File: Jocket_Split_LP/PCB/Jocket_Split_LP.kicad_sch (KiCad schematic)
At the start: 79 parts, among them J2 4PIN, J3 OLED, J4 53780-0270, P1 i2c_pin, P2 i2c_pin, SW1 SW_PUSH_LED, SW10 SW_PUSH_LED, SW11 SW_PUSH_LED, SW12 SW_PUSH_LED, SW13 SW_PUSH_LED, SW14 SW_PUSH_LED, SW15 SW_PUSH_LED, SW16 SW_PUSH_LED, SW17 SW_PUSH_LED, SW18 SW_PUSH_LED, SW19 SW_PUSH_LED, SW2 SW_PUSH_LED, SW20 SW_PUSH_LED, SW21 SW_PUSH_LED, SW22 SW_PUSH_LED, SW23 SW_PUSH_LED, SW24 SW_PUSH_LED, SW25 Rotary_Encoder_Switch, SW26 SW_PUSH_LED, SW27 SW_PUSH_LED, SW28 SW_PUSH_LED, SW29 SW_PUSH_LED, SW3 SW_PUSH_LED, SW30 SW_PUSH_LED, SW4 SW_PUSH_LED, SW5 SW_PUSH_LED, SW6 SW_PUSH_LED, SW7 SW_PUSH_LED, SW8 SW_PUSH_LED, SW9 SW_PUSH_LED, U1 ProMicro

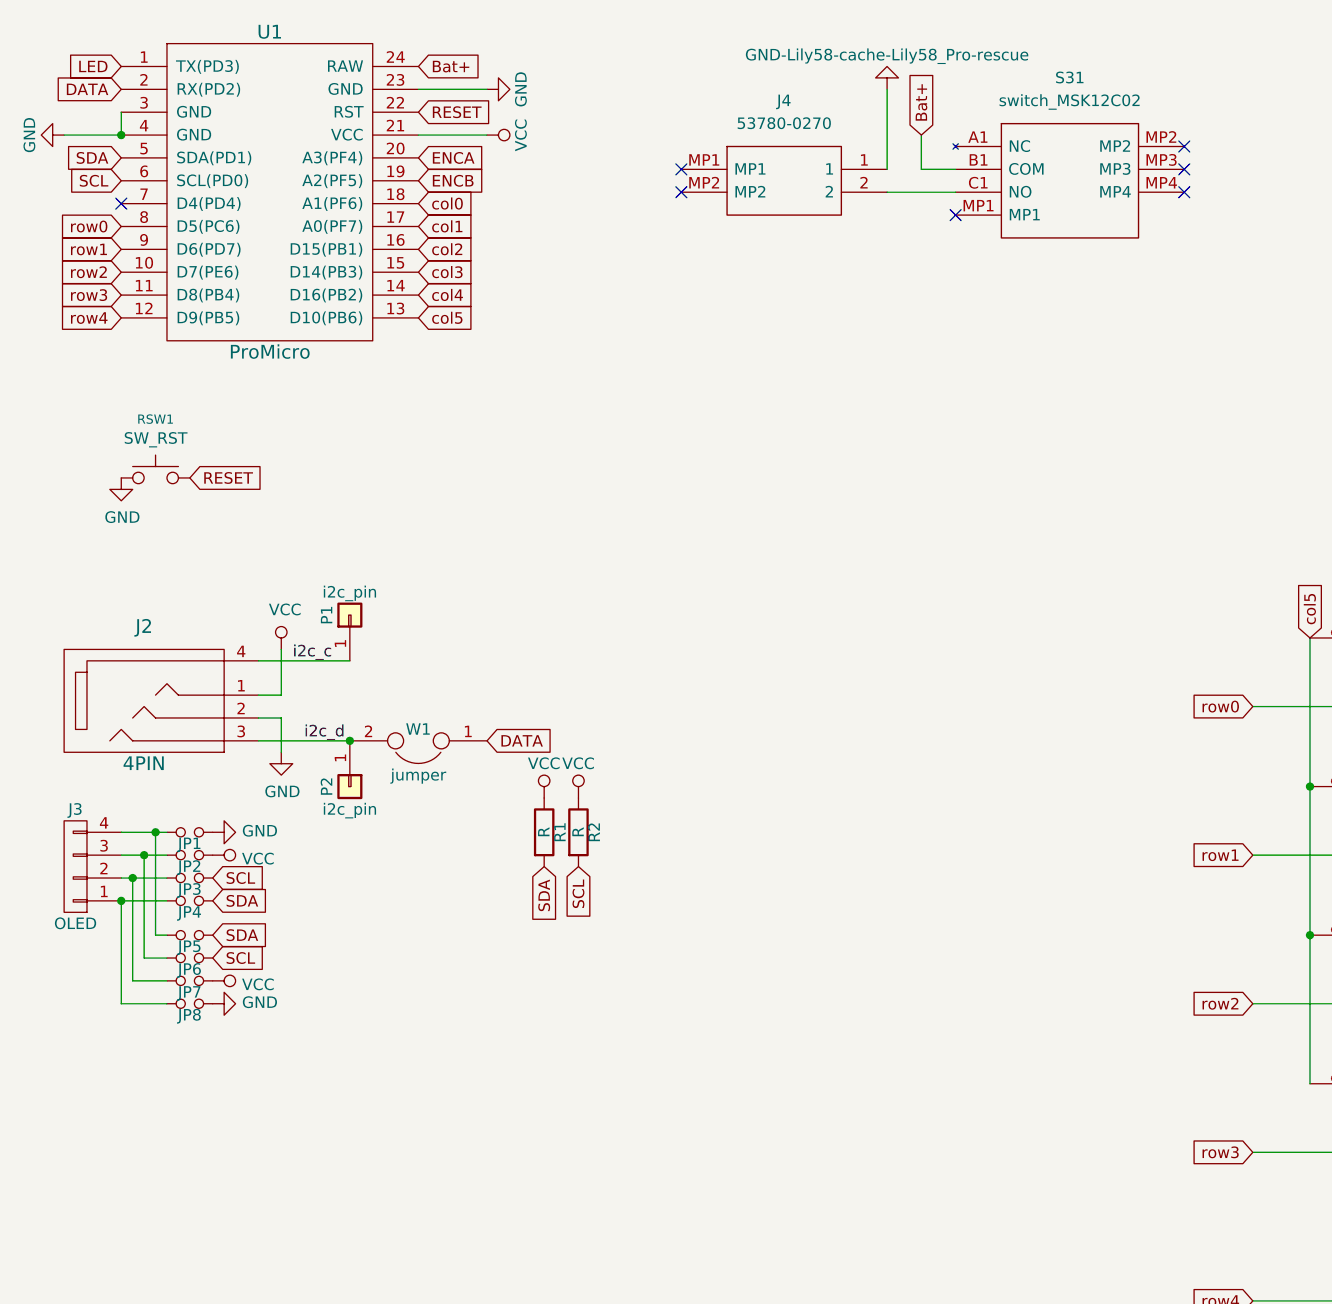
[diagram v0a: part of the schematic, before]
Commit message: General placement for components
Components in place, next step: routing
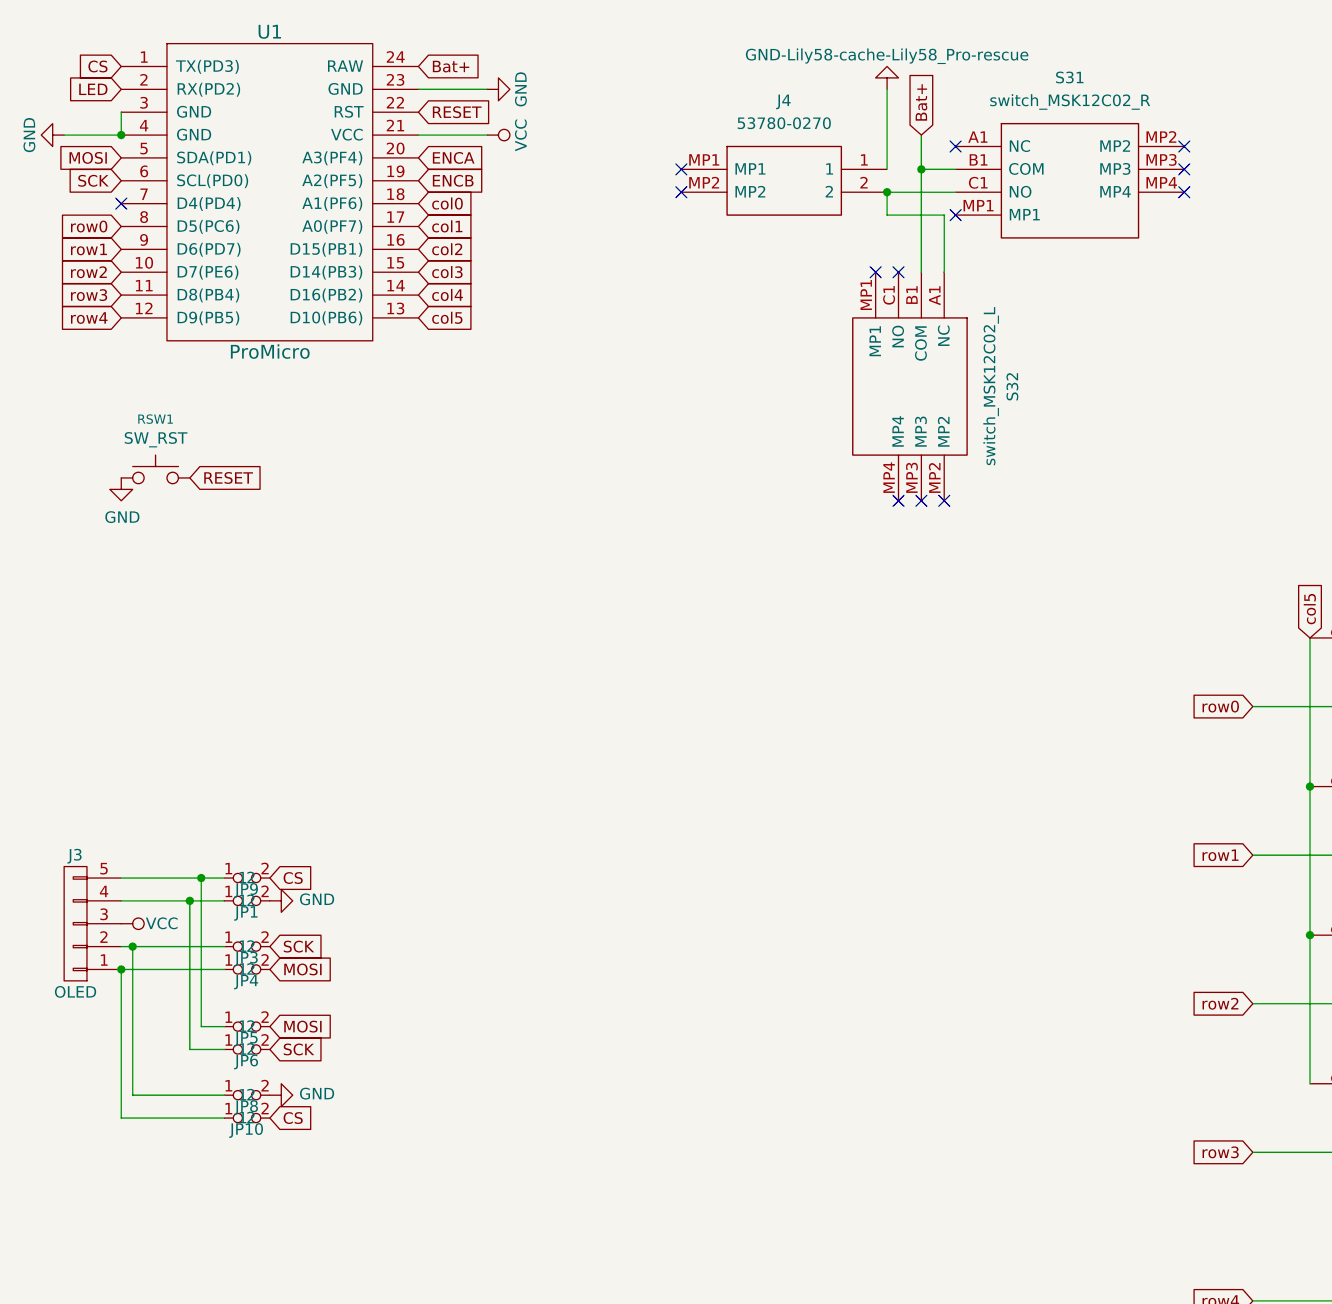
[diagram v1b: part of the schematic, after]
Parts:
- removed J2: 4PIN, Jocket_Split_LP-footprint:MJ-4PP-9, symbol Jocket_Split_LP-rescue:MJ-4PP-9-Lily58-cache-Lily58_Pro-rescue
- removed JP2, JP7: Jumper_NO_Small, Jocket_Split_LP-footprint:Jumper, symbol Jocket_Split_LP-rescue:Jumper_NO_Small-Device
- removed P1, P2: i2c_pin, Jocket_Split_LP-footprint:1pin_conn, symbol Jocket_Split_LP-rescue:i2c_pin-Lily58-cache-Lily58_Pro-rescue
- removed R1, R2: R, Jocket_Split_LP-footprint:RESISTOR_mini, symbol Jocket_Split_LP-rescue:R-Lily58-cache-Lily58_Pro-rescue
- removed W1: jumper, Jocket_Split_LP-footprint:jumper_data, symbol Jocket_Split_LP-rescue:Jumper
- added JP10, JP9: Jumper_NO_Small, Jocket_Split_LP-footprint:Jumper, symbol Jocket_Split_LP-rescue:Jumper_NO_Small-Device
- added S32: switch_MSK12C02_L, Jocket_Split_LP-footprint:Switch_MSK12C02, symbol Jocket_Split_LP-rescue:switch_MSK12C02
- J3: footprint Jocket_Split_LP-footprint:OLED_4Pin -> Jocket_Split_LP-footprint:OLED_Nice!View; symbol Jocket_Split_LP-rescue:OLED-Lily58-cache-Lily58_Pro-rescue -> Jocket_Split_LP-rescue:OLED-Nice!View
- S31: value switch_MSK12C02 -> switch_MSK12C02_R; footprint Jocket_Split_LP-footprint:Switch_MSK12C02_DoubleSided -> Jocket_Split_LP-footprint:Switch_MSK12C02
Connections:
- net DATA is gone; now on net LED: U1.2 (RX(PD2))
- net Bat+: now also S32.B1 (COM)
- net LED: no longer U1.1 (TX(PD3))
- net VCC: now also J3.3 (P3)
- net at J4.2, S31.C1 (NO): now also S32.A1 (NC)
- net at J3.2 (P2), JP3.1: now also JP8.1
- net at J3.4 (P4), JP1.1: now also JP6.1; no longer JP5.1
- net at J3.1 (P1), JP4.1: now also JP10.1; no longer JP8.1
- net SCL renamed SCK
- net SDA renamed MOSI
- new net: J3.5 (P5), JP5.1, JP9.1
- new net CS: JP10.2, JP9.2, U1.1 (TX(PD3))
- no-connect marks 8 -> 14

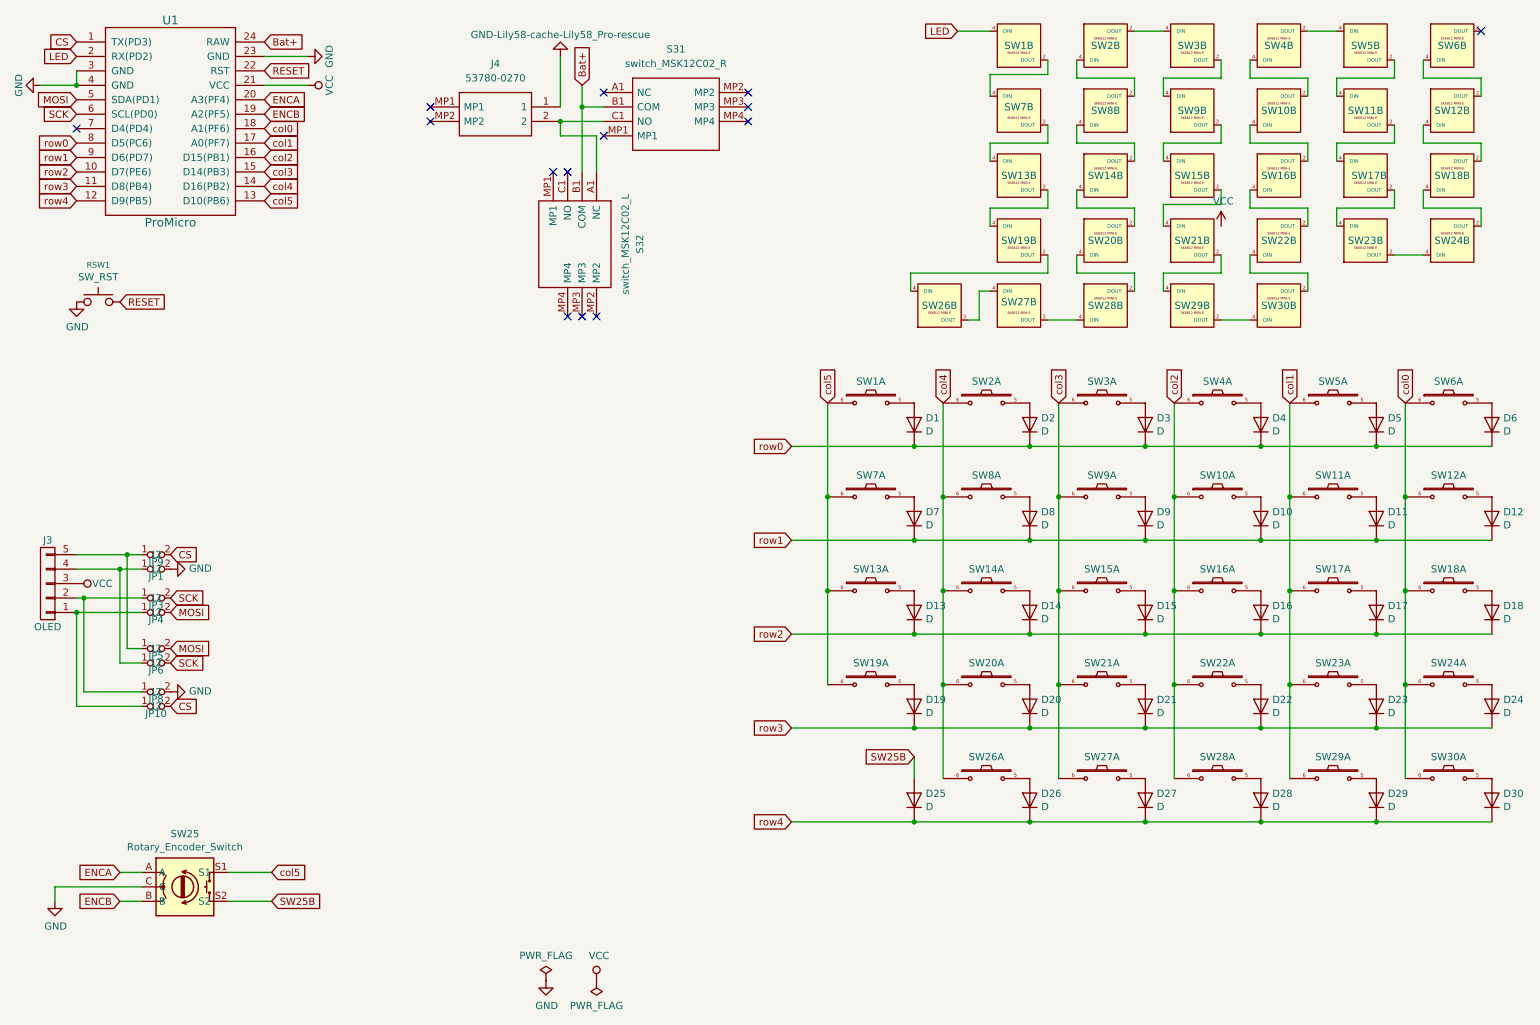
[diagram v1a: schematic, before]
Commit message: Traces and case updated
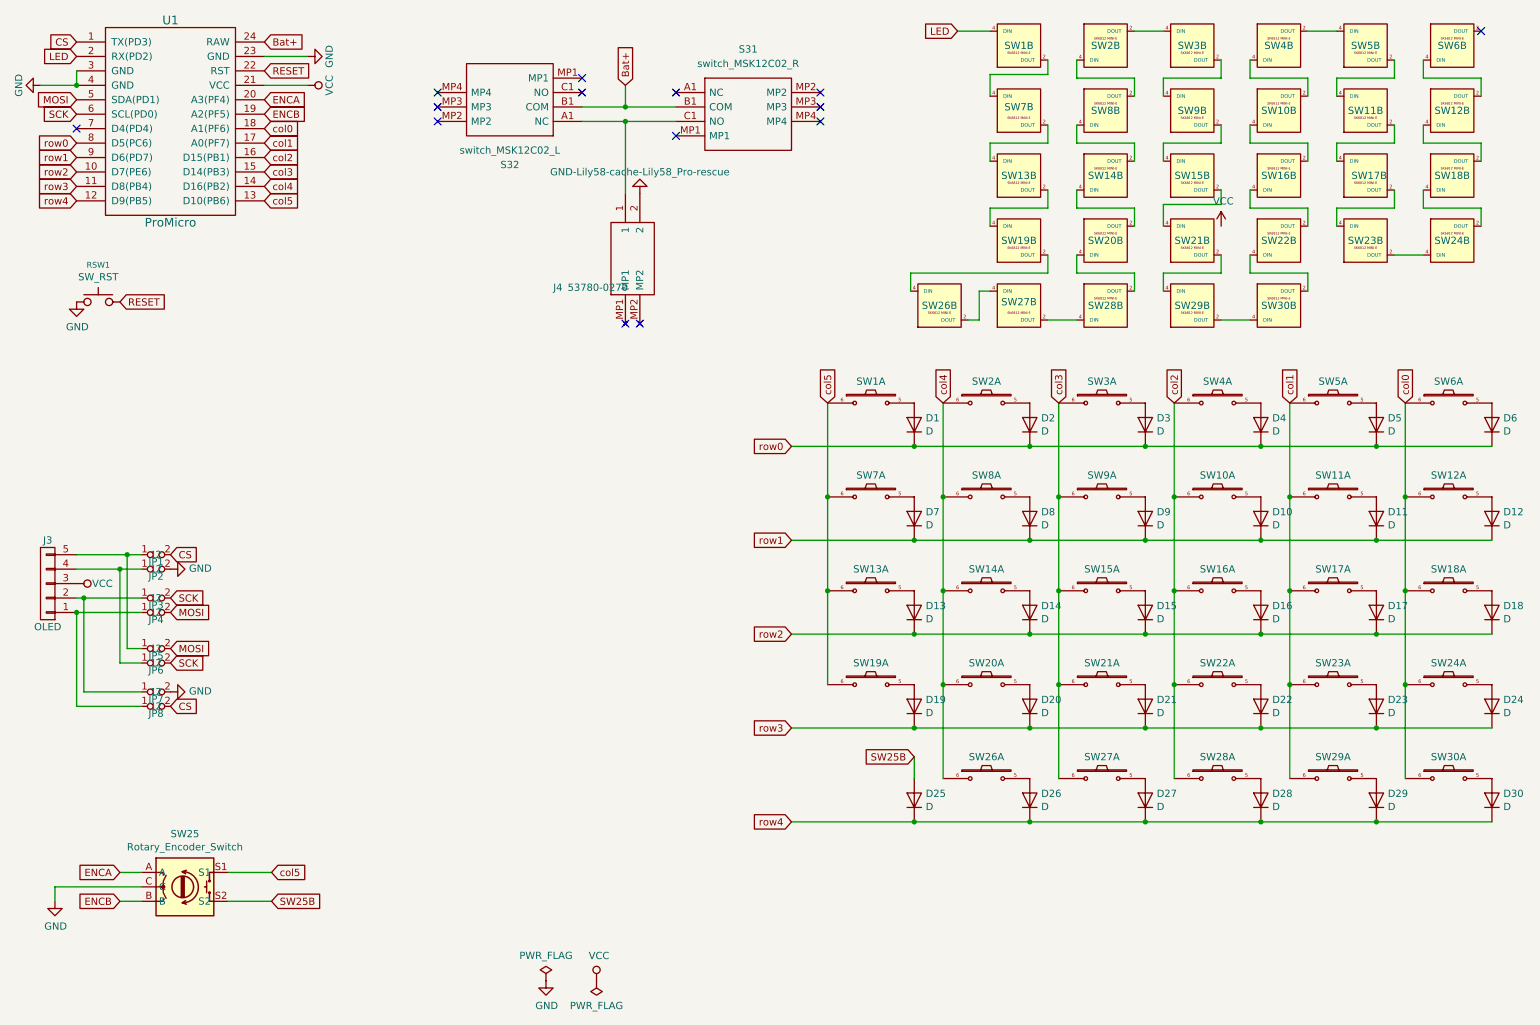
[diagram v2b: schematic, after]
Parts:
- renumbered JP9 to JP1, JP1 to JP2, JP8 to JP7, JP10 to JP8
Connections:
- net GND: now also J4.2; no longer J4.1
- net at S31.C1 (NO), S32.A1 (NC): now also J4.1; no longer J4.2
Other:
- moved on the sheet: S31, S32
